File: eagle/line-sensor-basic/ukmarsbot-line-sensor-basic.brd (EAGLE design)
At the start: 99.1 x 25.4 mm, 25 parts, among them Q1 PN2222A*, T1 BPW96B, T2 BPW96B, T3 BPW96B, T4 BPW96B

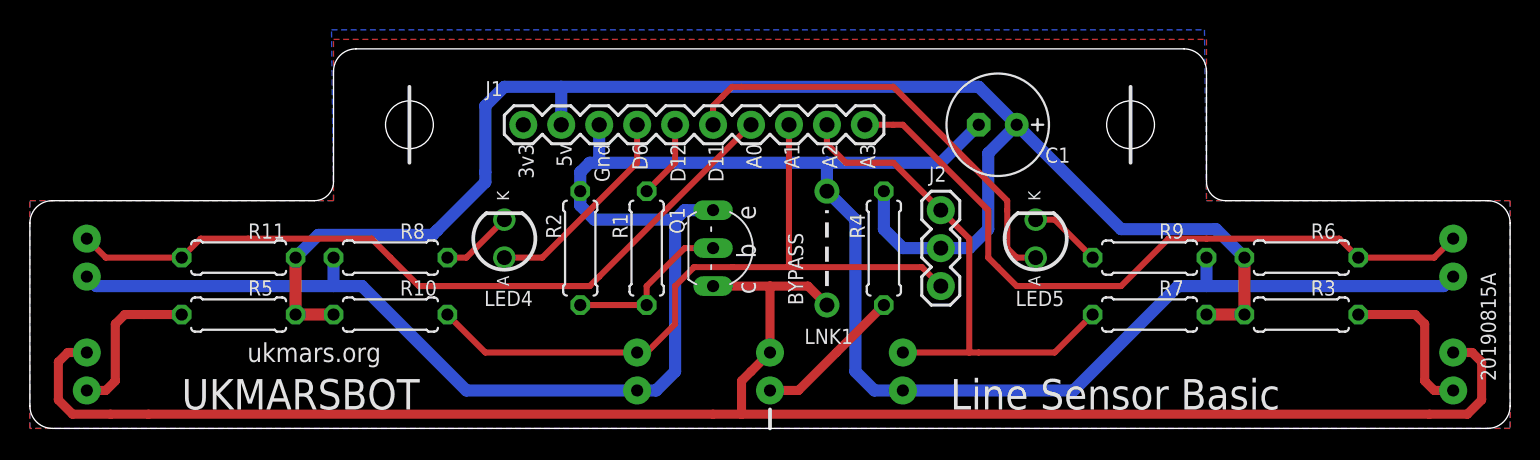
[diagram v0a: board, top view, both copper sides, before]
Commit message: Update Line Sensor Basic and library with larger pads/holes for parts
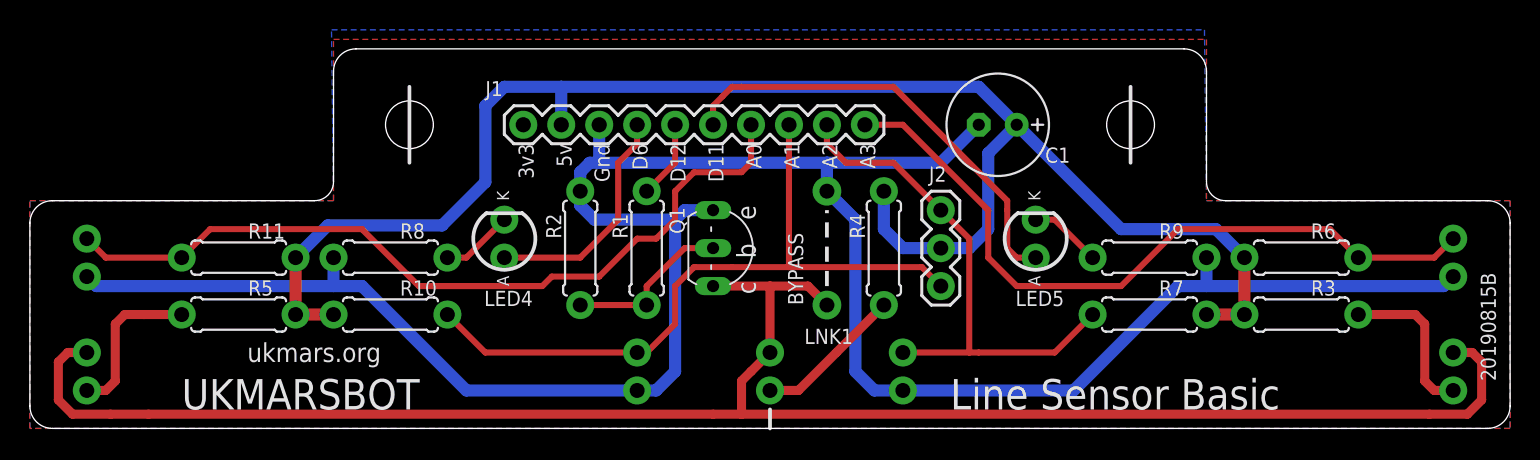
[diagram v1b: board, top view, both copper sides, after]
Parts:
- Q1: value PN2222A* -> BC337*
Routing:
- net A0: track 51.3 -> 54.4 mm
- net D6: track 14.1 -> 15.5 mm
- net A3: track 48.1 -> 48.6 mm
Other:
- board text added: "20190815B"
- board text removed: "20190815A"

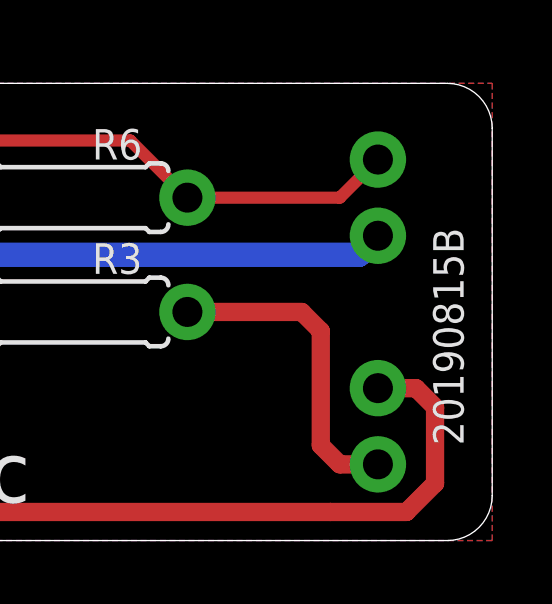
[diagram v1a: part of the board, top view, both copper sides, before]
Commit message: Removed references to depracated SFH4550
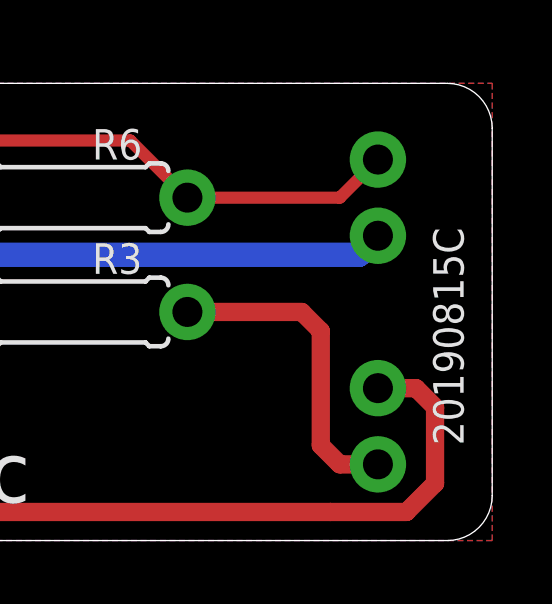
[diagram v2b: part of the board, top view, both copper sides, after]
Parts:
- LED1, LED2, LED3: value SFH4550 -> Emitter
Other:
- board text added: "20190815C"
- board text removed: "20190815B"
